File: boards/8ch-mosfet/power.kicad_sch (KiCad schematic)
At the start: 21 parts, among them J3 Screw_Terminal_01x08, J4 Screw_Terminal_01x08, U21 XL1509-5.0

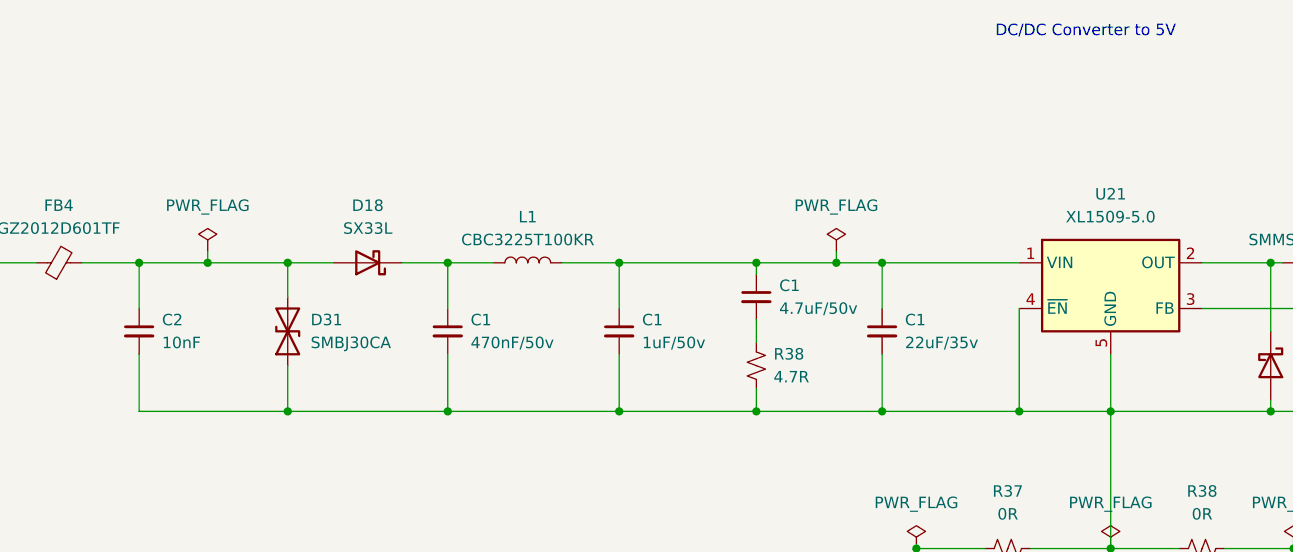
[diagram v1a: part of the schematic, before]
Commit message: first commit of the 'totem pole' driver design
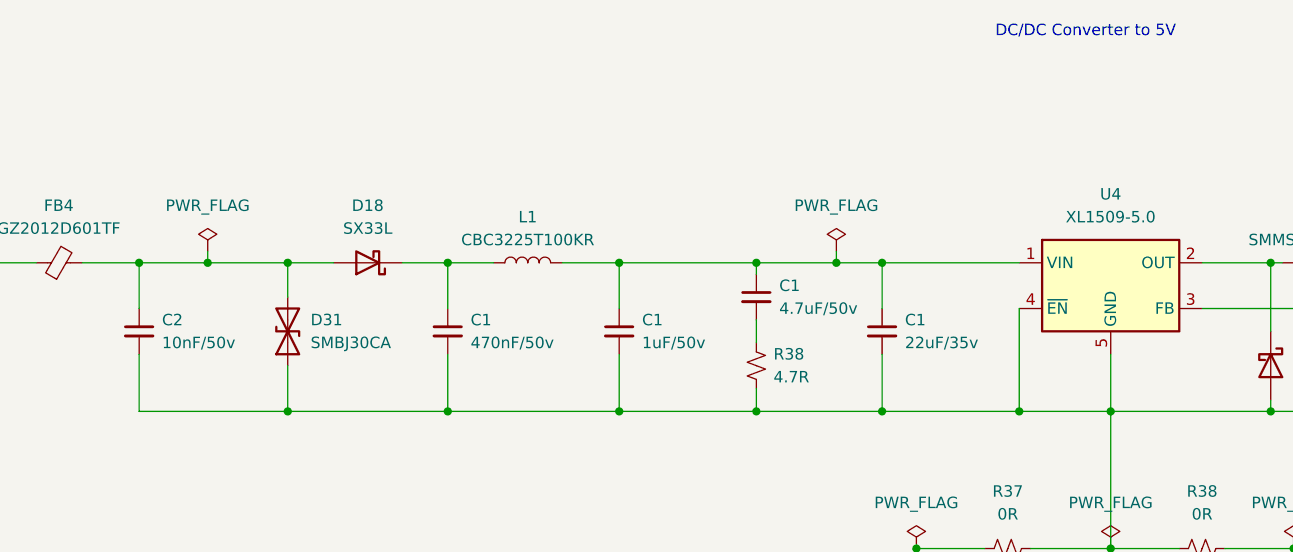
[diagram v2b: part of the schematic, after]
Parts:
- C2: value 10nF -> 10nF/50v
- L2: footprint Inductor_SMD:L_Chilisin_BMRB00060650 -> Inductor_SMD:L_Chilisin_BMRA00040420
- renumbered U21 to U4

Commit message: updated inductor footprint
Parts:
- L2: footprint Inductor_SMD:L_Chilisin_BMRA00040420 -> Inductor_SMD:L_Chilisin_BMRB00060650
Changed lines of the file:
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@@
       (effects (font (size 1.27 1.27)))
     )
-    (property "Footprint" "Inductor_SMD:L_Chilisin_BMRA00040420" (at 200.66 80.01 0)
+    (property "Footprint" "Inductor_SMD:L_Chilisin_BMRB00060650" (at 200.66 80.01 0)
       (effects (font (size 1.27 1.27)) hide)
     )

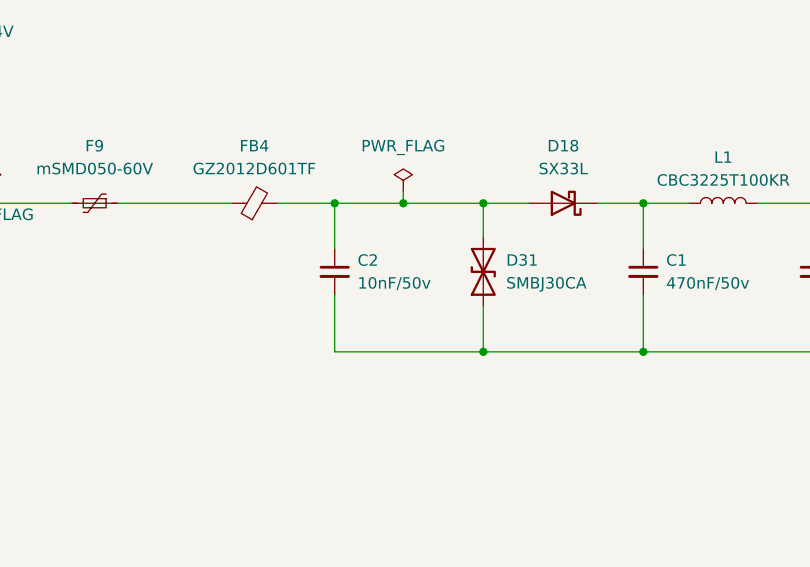
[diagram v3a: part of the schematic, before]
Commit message: updated mosfet driver schematic with changes
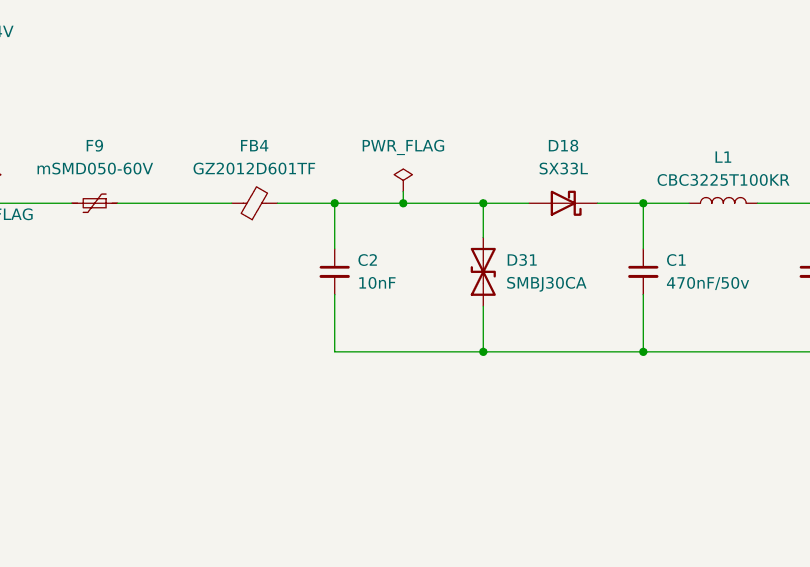
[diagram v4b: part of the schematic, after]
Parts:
- C2: value 10nF/50v -> 10nF
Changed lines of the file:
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@@
       (effects (font (size 1.27 1.27)) (justify left))
     )
-    (property "Value" "10nF/50v" (at 72.39 88.9063 0)
+    (property "Value" "10nF" (at 72.39 88.9063 0)
       (effects (font (size 1.27 1.27)) (justify left))
     )

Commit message: reannotated
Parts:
- renumbered U4 to U21
